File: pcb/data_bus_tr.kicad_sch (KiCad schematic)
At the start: 9 parts, among them U19 74LS245, U20 74LS245, U5 74LS245, U6 74LS245, U7 74LS245, U8 74LS245

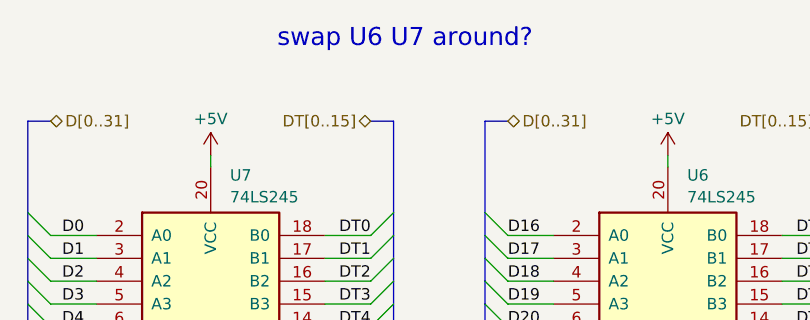
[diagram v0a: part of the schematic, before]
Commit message: removing obsolete schematic comment
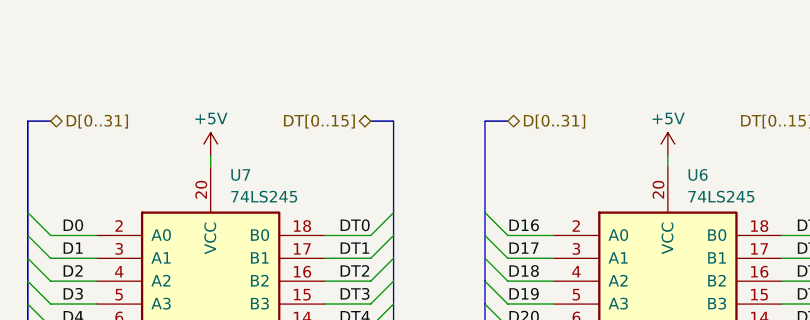
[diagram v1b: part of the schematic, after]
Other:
- note removed: "swap U6 U7 around?"
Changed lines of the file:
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@@
 		(company "maniek86.xyz")
-	)
-	(text "swap U6 U7 around?"
-		(exclude_from_sim no)
-		(at 85.09 18.796 0)
-		(effects
-			(font
-				(size 2 2)
-			)
-		)
 	)
 	(text "W/R#,\n0 - Read B<A\n1 - Write A>B"

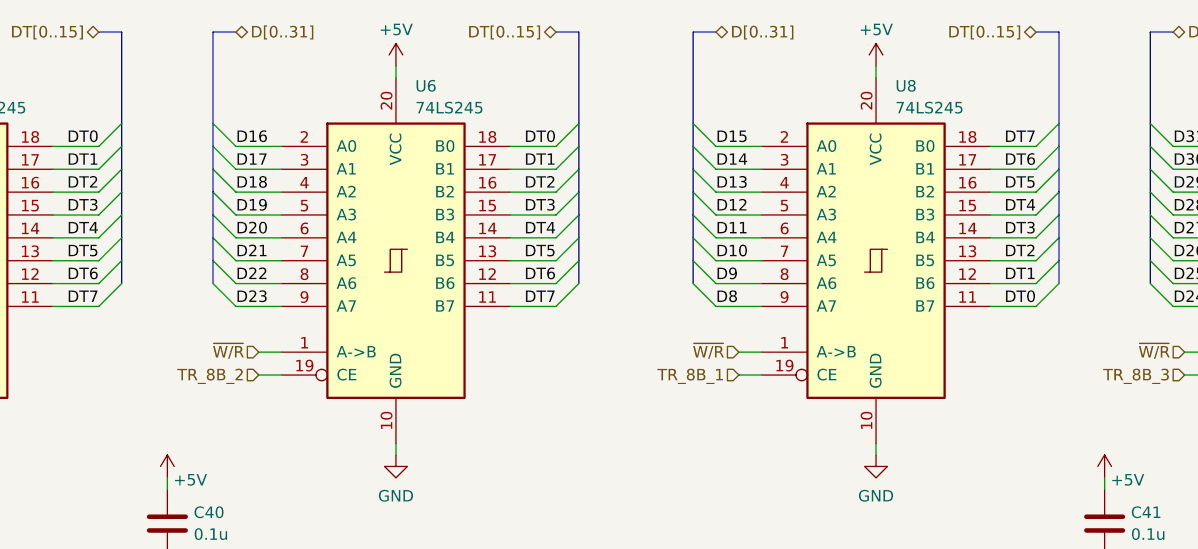
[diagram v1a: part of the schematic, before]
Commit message: data_bus_tr paired up, correct decoupling caps per pair
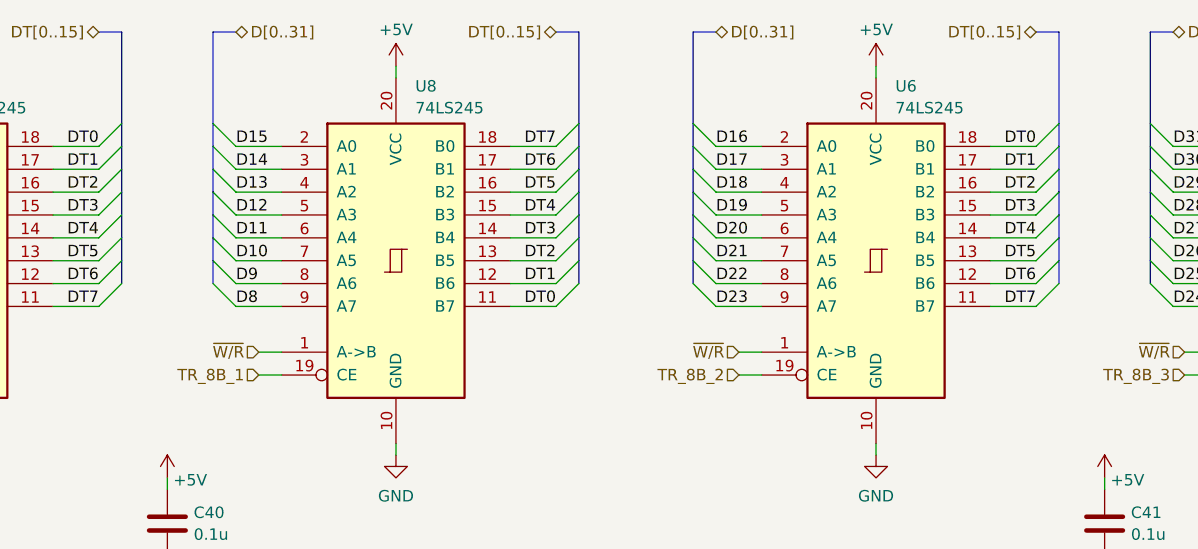
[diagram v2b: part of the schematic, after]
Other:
- moved on the sheet: U6, U8
